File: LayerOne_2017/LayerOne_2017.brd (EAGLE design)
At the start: 80 x 73.7 mm, 48 parts, among them IC1 STM32F446_LQFP64, IC2 REG1117, J1 SPI_TFT_DISPLAY, Q1 2N2222, Q2 MMBT2222A, U1 SN65HVD235DR, U2 SN65HVD235DR, U4 SDCARD, X1 STEREOJACK, X2 MINI-USB-32005-301

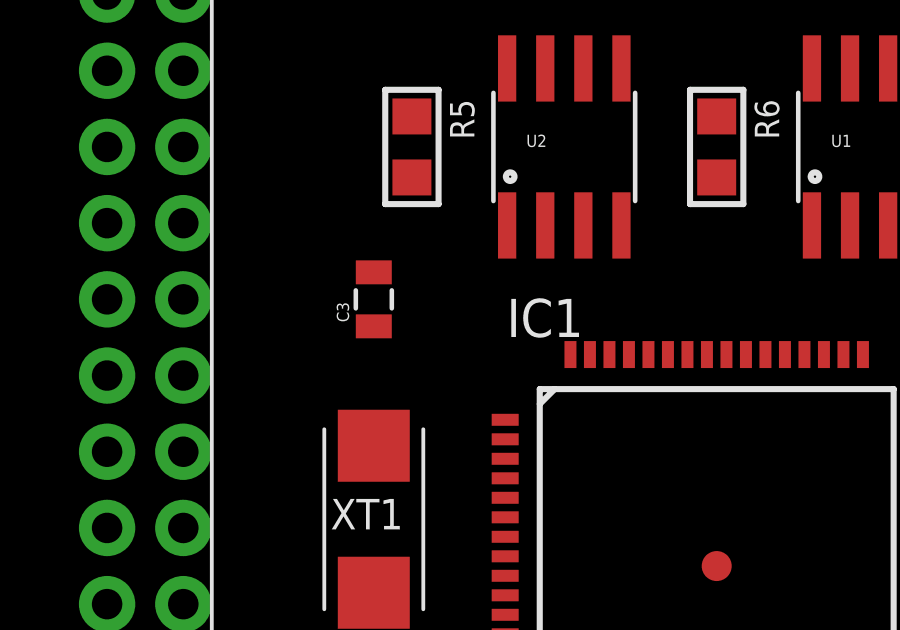
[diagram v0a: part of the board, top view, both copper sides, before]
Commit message: 
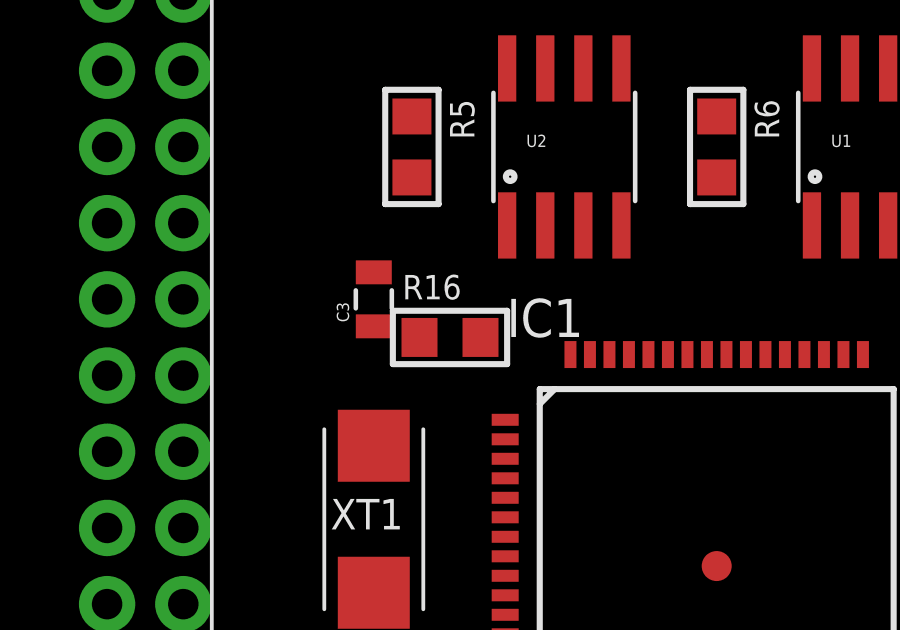
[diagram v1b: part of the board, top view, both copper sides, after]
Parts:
- added R16: 220, microbuilder:_0805
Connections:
- new net N$19: IC1.5, R16.2
- net N$18: now also R16.1; no longer IC1.5
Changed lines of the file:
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@@
 <?xml version="1.0" encoding="utf-8"?>
 <!DOCTYPE eagle SYSTEM "eagle.dtd">
-<eagle version="7.6.0">
+<eagle version="7.7.0">
 <drawing>
 <settings>
@@
 <element name="R15" library="microbuilder" package="_0805" value="1K" x="8.89" y="12.7" rot="R90"/>
 <element name="CN1" library="microbuilder" package="USB_HOST-PTH" value="" x="52.07" y="5.08"/>
+<element name="R16" library="microbuilder" package="_0805" value="220" x="24.13" y="48.26"/>
 </elements>
 <signals>
@@
 <wire x1="21.59" y1="50.43" x2="22.86" y2="53.594" width="0" layer="19" extent="1-1"/>
 <wire x1="15.24" y1="57.15" x2="22.86" y2="53.594" width="0" layer="19" extent="1-1"/>
+<wire x1="8.6106" y1="65.3796" x2="15.24" y2="57.15" width="0" layer="19" extent="1-1"/>
+<wire x1="10.16" y1="68.45" x2="8.6106" y2="65.3796" width="0" layer="19" extent="1-1"/>
 <wire x1="15.24" y1="41.91" x2="21.59" y2="50.43" width="0" layer="19" extent="1-1"/>
 <wire x1="15.24" y1="39.37" x2="15.24" y2="41.91" width="0" layer="19" extent="1-1"/>
@@
 <wire x1="28.795" y1="33.59" x2="21.59" y2="34.66" width="0" layer="19" extent="1-1"/>
 <wire x1="37.245" y1="33.59" x2="28.795" y2="33.59" width="0" layer="19" extent="1-1"/>
-<wire x1="10.16" y1="68.45" x2="15.24" y2="57.15" width="0" layer="19" extent="1-1"/>
-<wire x1="8.6106" y1="65.3796" x2="10.16" y2="68.45" width="0" layer="19" extent="1-1"/>
 <wire x1="3.81" y1="50.67" x2="15.24" y2="57.15" width="0" layer="19" extent="1-1"/>
 <wire x1="29.99" y1="14.84" x2="28.795" y2="33.59" width="0" layer="19" extent="1-1"/>
@@
 </signal>
 <signal name="N$18">
-<contactref element="IC1" pad="5"/>
 <contactref element="C3" pad="1"/>
 <contactref element="XT1" pad="A"/>
-<wire x1="21.59" y1="44.65" x2="21.59" y2="48.63" width="0" layer="19" extent="1-1"/>
-<wire x1="25.97" y1="42.915" x2="21.59" y2="44.65" width="0" layer="19" extent="1-1"/>
+<contactref element="R16" pad="1"/>
+<wire x1="21.59" y1="48.63" x2="23.114" y2="48.26" width="0" layer="19" extent="1-1"/>
+<wire x1="21.59" y1="44.65" x2="23.114" y2="48.26" width="0" layer="19" extent="1-1"/>
 </signal>
 <signal name="DAC_OUT1">
@@
 <contactref element="R15" pad="1"/>
 </signal>
+<signal name="N$19">
+<contactref element="IC1" pad="5"/>
+<contactref element="R16" pad="2"/>
+<wire x1="25.97" y1="42.915" x2="25.146" y2="48.26" width="0" layer="19" extent="1-1"/>
+</signal>
 </signals>

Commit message: usb changes
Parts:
- added R17, R18: 22, microbuilder:_0805
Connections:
- removed net N$7: IC1.35
- removed net N$8: IC1.36
- new net USB_OTG_HS_DM: IC1.35, R18.2
- new net USB_OTG_HS_DP: IC1.36, R17.2
- net HOST_D+: now also R17.1
- net HOST_D-: now also R18.1
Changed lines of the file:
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@@
 <element name="CN1" library="microbuilder" package="USB_HOST-PTH" value="" x="52.07" y="5.08"/>
 <element name="R16" library="microbuilder" package="_0805" value="220" x="24.13" y="48.26"/>
+<element name="R17" library="microbuilder" package="_0805" value="22" x="69.85" y="15.24" rot="R90">
+<attribute name="DIGIKEY" value="RMCF0603JT10K0CT-ND" x="69.85" y="15.24" size="1.778" layer="27" rot="R90" display="off"/>
+<attribute name="OC_NEWARK" value="unknown" x="69.85" y="15.24" size="1.778" layer="27" rot="R90" display="off"/>
+<attribute name="MF" value="" x="69.85" y="15.24" size="1.778" layer="27" rot="R90" display="off"/>
+<attribute name="MPN" value="RMCF0603JT10K0" x="69.85" y="15.24" size="1.778" layer="27" rot="R90" display="off"/>
+<attribute name="PARTNO" value="RMCF0603JT10K0" x="69.85" y="15.24" size="1.778" layer="27" rot="R90" display="off"/>
+</element>
+<element name="R18" library="microbuilder" package="_0805" value="22" x="67.31" y="15.24" rot="R90">
+<attribute name="DIGIKEY" value="RMCF0603JT10K0CT-ND" x="67.31" y="15.24" size="1.778" layer="27" rot="R90" display="off"/>
+<attribute name="OC_NEWARK" value="unknown" x="67.31" y="15.24" size="1.778" layer="27" rot="R90" display="off"/>
+<attribute name="MF" value="" x="67.31" y="15.24" size="1.778" layer="27" rot="R90" display="off"/>
+<attribute name="MPN" value="RMCF0603JT10K0" x="67.31" y="15.24" size="1.778" layer="27" rot="R90" display="off"/>
+<attribute name="PARTNO" value="RMCF0603JT10K0" x="67.31" y="15.24" size="1.778" layer="27" rot="R90" display="off"/>
+</element>
 </elements>
 <signals>
@@
 <signal name="HOST_D+">
 <contactref element="X2" pad="3"/>
+<contactref element="R17" pad="1"/>
+<wire x1="68.58" y1="8.08" x2="69.85" y2="14.224" width="0" layer="19" extent="1-1"/>
 </signal>
 <signal name="HOST_D-">
 <contactref element="X2" pad="2"/>
+<contactref element="R18" pad="1"/>
+<wire x1="67.78" y1="8.08" x2="67.31" y2="14.224" width="0" layer="19" extent="1-1"/>
 </signal>
 <signal name="SLOPE2">
@@
 <signal name="N$6">
 <contactref element="IC1" pad="34"/>
-</signal>
-<signal name="N$7">
-<contactref element="IC1" pad="35"/>
-</signal>
-<signal name="N$8">
-<contactref element="IC1" pad="36"/>
 </signal>
 <signal name="N$25">
@@
 <wire x1="25.97" y1="42.915" x2="25.146" y2="48.26" width="0" layer="19" extent="1-1"/>
 </signal>
+<signal name="USB_OTG_HS_DP">
+<contactref element="R17" pad="2"/>
+<contactref element="IC1" pad="36"/>
+<wire x1="40.07" y1="37.715" x2="69.85" y2="16.256" width="0" layer="19" extent="1-1"/>
+</signal>
+<signal name="USB_OTG_HS_DM">
+<contactref element="R18" pad="2"/>
+<contactref element="IC1" pad="35"/>
+<wire x1="40.07" y1="37.065" x2="67.31" y2="16.256" width="0" layer="19" extent="1-1"/>
+</signal>
 </signals>

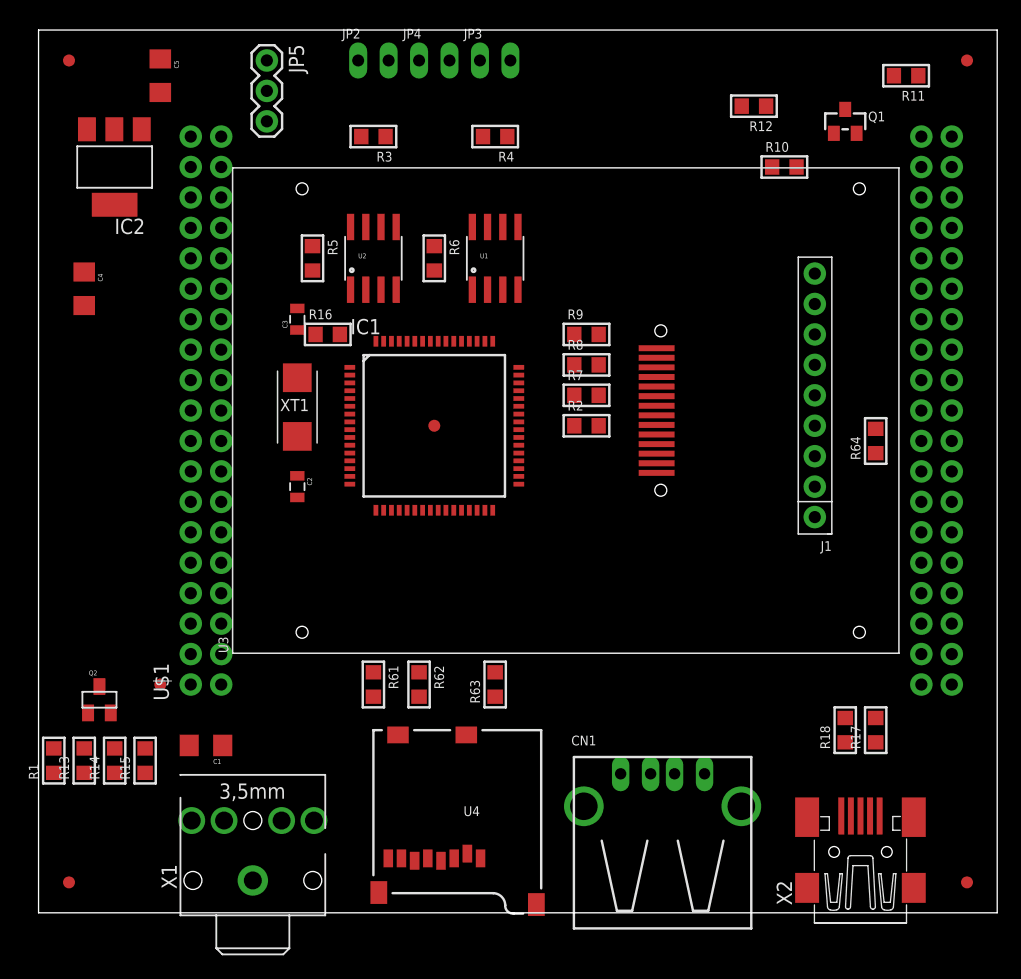
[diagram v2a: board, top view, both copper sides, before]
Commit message: 
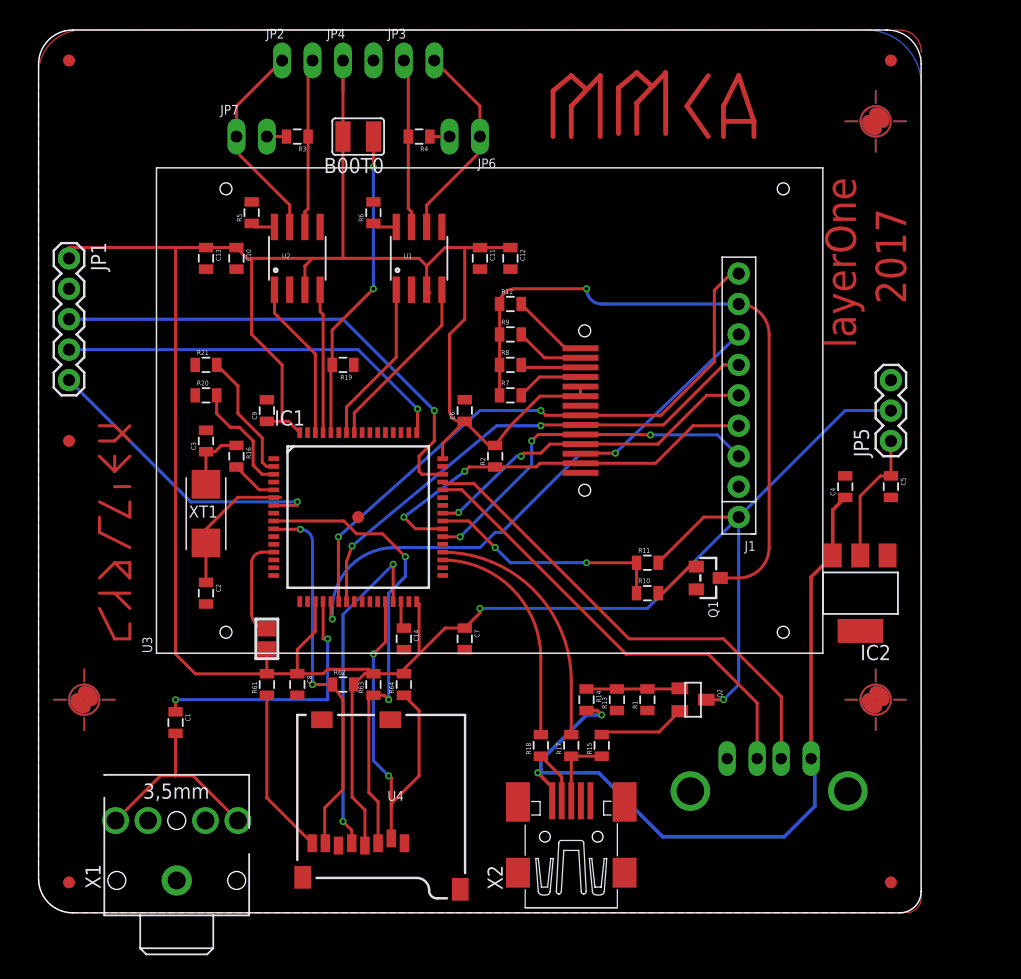
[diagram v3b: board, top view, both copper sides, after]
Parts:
- removed U$1: MOPHOMOPHO_466RE, mopho:MOPHO
- added B00T0: (no value), jumper:SJW
- added C10, C12: 100nF, SparkFun-Capacitors:0805
- added C11, C13: 1uF, SparkFun-Capacitors:0805
- added C14: 4.7uF/X7R, SparkFun-Passives:0805
- added C6, C7, C8, C9: 100nF, SparkFun-Passives:0805
- added FID1, FID2, FID3: FIDUCIALROUND, microbuilder:PASS-ROUND
- added JP1: (no value), SparkFun:1X05
- added JP6, JP7: (no value), microbuilder:1X02_OVAL
- added R19, R20, R21: 10K, SparkFun-Passives:0805
- added U5: FERRITE0805, STM32-PROX:RLC_0805
- C1: device SparkFun:1206 -> SparkFun-Passives:0805
- C2, C3: device SparkFun:0805 -> SparkFun-Passives:0805
- C4, C5: value (none) -> 1uF; device SparkFun:1206 -> SparkFun-Passives:0805
- R1, R10: value 1K -> 100; device microbuilder:_0805 -> SparkFun-Passives:0805
- R11, R12, R16, R17, R18, R2, R3, R4, R5, R6, R61, R62, R63, R64, R7, R8, R9: device microbuilder:_0805 -> SparkFun-Passives:0805
- R13: value 1K -> 36K; device microbuilder:_0805 -> SparkFun-Passives:0805
- R14: value 1K -> 10K; device microbuilder:_0805 -> SparkFun-Passives:0805
- R15: value 1K -> 1K5; device microbuilder:_0805 -> SparkFun-Passives:0805
- moved IC2 71.7 mm to (68.6, 26.7)
- moved C5 69.9 mm to (71.1, 35.6)
- moved C4 65.6 mm to (67.3, 35.6), turned to 90 degrees
- moved JP5 61.0 mm to (71.1, 39.4), turned to 90 degrees
- moved R1 49.8 mm to (50.8, 17.8)
- moved Q2 49.5 mm to (54.6, 17.8), turned to 270 degrees
- moved R11 46.0 mm to (50.8, 29.2), turned to 0 degrees
- moved R13 44.7 mm to (48.3, 17.8)
- moved R64 44.3 mm to (30.5, 19.1)
- moved Q1 39.8 mm to (55.9, 27.9), turned to 270 degrees
- moved R14 39.7 mm to (45.7, 17.8), turned to 270 degrees
- moved R15 38.1 mm to (47.0, 14.0)
- moved R10 37.4 mm to (50.8, 26.7)
- moved R12 26.2 mm to (39.4, 50.8), turned to 0 degrees
- moved R18 25.4 mm to (41.9, 14.0)
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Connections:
- net N$5 renamed USB_RENUM
- removed net N$11: R13.1
- removed net N$12: R15.1
- removed net N$25: IC1.24
- removed net N$9: R14.2
- removed net VBAT: U$1.P$33
- removed net VDD: U$1.P$5
- removed net VDDA: IC1.13
- removed net VIN: U$1.P$24
- removed net VSSA: IC1.12
- new net B00T0: B00T0.1, IC1.60, R19.2
- new net N$22: JP6.2, R4.1
- new net NRST: IC1.7, JP1.5
- new net SELECT0: IC1.2, R21.2
- new net SELECT1: IC1.3, R20.2
- net !SD_CS: now also IC1.28; no longer IC1.33, U$1.P$59
- net +3V3: now also B00T0.2, C10.1, C11.1, C12.1, C13.1, C6.1, C7.1, C8.1, C9.1, JP1.1, Q2.3, U5.2
- net AVDD: now also IC1.13, U5.1; no longer U$1.P$45
- net CAN1_RX: no longer U$1.P$41
- net CAN1_TX: no longer U$1.P$43
- net CAN2_RX: no longer U$1.P$67
- net CAN2_TX: no longer U$1.P$55
- net CANH1: now also JP7.1; no longer R3.2
- net CANL2: now also JP6.1; no longer R4.1
- net D+: no longer U$1.P$50
- net D-: no longer U$1.P$52
- net DAC_OUT1: no longer U$1.P$32
- net GND: now also C10.2, C11.2, C12.2, C13.2, C14.2, C6.2, C7.2, C8.2, C9.2, IC1.12, JP1.2, JP4.2, R13.1, R19.1, R20.1, R21.1; no longer U$1.P$20, U$1.P$22, U$1.P$47, U$1.P$58, U$1.P$8
- net HOST_D+: now also R15.1
- net MORPHO_+3V3: no longer U$1.P$16
- net N$2: now also C14.1, IC1.30; no longer Q2.3
- net N$6: now also JP7.2, R3.2; no longer IC1.34
- net SD_MISO: no longer U$1.P$66
- net SD_MOSI: no longer U$1.P$64
- net SD_SCK: no longer U$1.P$68
- net SYS_JTCK-SWCLK: now also JP1.4
- net SYS_JTMS-SWDIO: now also JP1.3
- net TFT_BACKLIGHT: now also IC1.40; no longer U$1.P$39
- net TFT_CS: no longer U$1.P$57
- net TFT_DC: no longer U$1.P$61
- net TFT_LCD: no longer IC1.40
- net TFT_MISO: no longer U$1.P$51
- net TFT_MOSI: no longer U$1.P$53
- net TFT_RESET: now also IC1.39; no longer IC1.16, U$1.P$73
- net TFT_SCK: no longer U$1.P$49
- net USB_ID: no longer U$1.P$71, X2.4
- net VCC: now also R14.2; no longer U$1.P$18
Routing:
- net +3V3: track 0.00 -> 272.6 mm, vias 0 -> 2
- net VCC: track 0.00 -> 65.5 mm, vias 0 -> 2
- net TFT_LCD: track 0.00 -> 55.1 mm, vias 0 -> 1
- net TFT_MISO: track 0.00 -> 51.4 mm, vias 0 -> 2
- net TFT_SCK: track 0.00 -> 48.5 mm, vias 0 -> 2
- net TFT_MOSI: track 0.00 -> 42.7 mm, vias 0 -> 2
- net SYS_JTMS-SWDIO: track 0.00 -> 41.3 mm, vias 0 -> 1
- net D+: track 0.00 -> 40.8 mm
- net SD_MOSI: track 0.00 -> 39.0 mm, vias 0 -> 2
- net D-: track 0.00 -> 38.3 mm
- net TFT_RESET: track 0.00 -> 34.4 mm, vias 0 -> 2
- net SYS_JTCK-SWCLK: track 0.00 -> 33.1 mm, vias 0 -> 1
- net SD_MISO: track 0.00 -> 31.4 mm, vias 0 -> 2
- net !SD_CS: track 0.00 -> 31.3 mm, vias 0 -> 2
- net TFT_CS: track 0.00 -> 30.2 mm, vias 0 -> 3
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- added copper zone on layer 1, net GND
- added copper zone on layer 16, net GND
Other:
- board size 80 x 73.7 mm -> 73.6 x 73.7 mm
- board text added: "2017"
- board text added: "layerOne"

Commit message: revised submission to itead
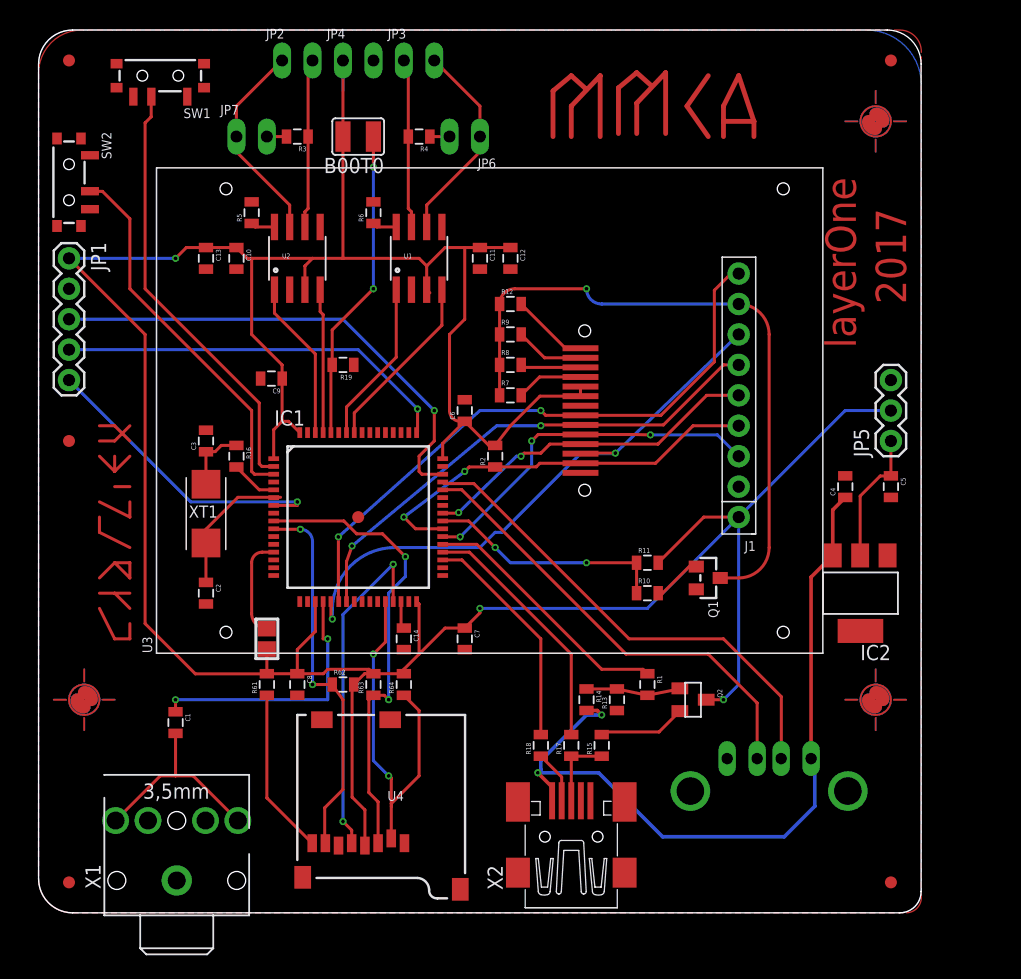
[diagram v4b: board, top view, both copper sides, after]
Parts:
- removed R20, R21: 10K, SparkFun-Passives:0805
- added SW1, SW2: (no value), microbuilder:SPST_SMT_19192
- moved C9 2.69 mm to (19.4, 44.6), turned to 180 degrees
- moved R1 1.27 mm to (50.8, 19.1), turned to 270 degrees
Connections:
- net +3V3: now also IC1.1
- net GND: now also SW1.C, SW2.C; no longer R20.1, R21.1
- net SELECT0: now also SW1.B; no longer R21.2
- net SELECT1: now also SW2.B; no longer R20.2
- net USB_RENUM: now also IC1.37
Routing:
- net SELECT0: track 10.8 -> 36.1 mm
- net SELECT1: track 9.58 -> 31.5 mm
- net USB_RENUM: track 0.00 -> 21.6 mm
- net +3V3: track 272.6 -> 277.0 mm, vias 2 -> 3
- net USB_OTG_HS_DP: track 19.7 -> 21.0 mm
- net USB_OTG_HS_DM: track 18.0 -> 18.9 mm
